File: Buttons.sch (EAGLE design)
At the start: 67 parts, among them J1 AVR_SPI_PROG_3X2TESTPOINTS, T1 SI2301, U1 TCA8418RTWR, U3 ATTINY88-MU

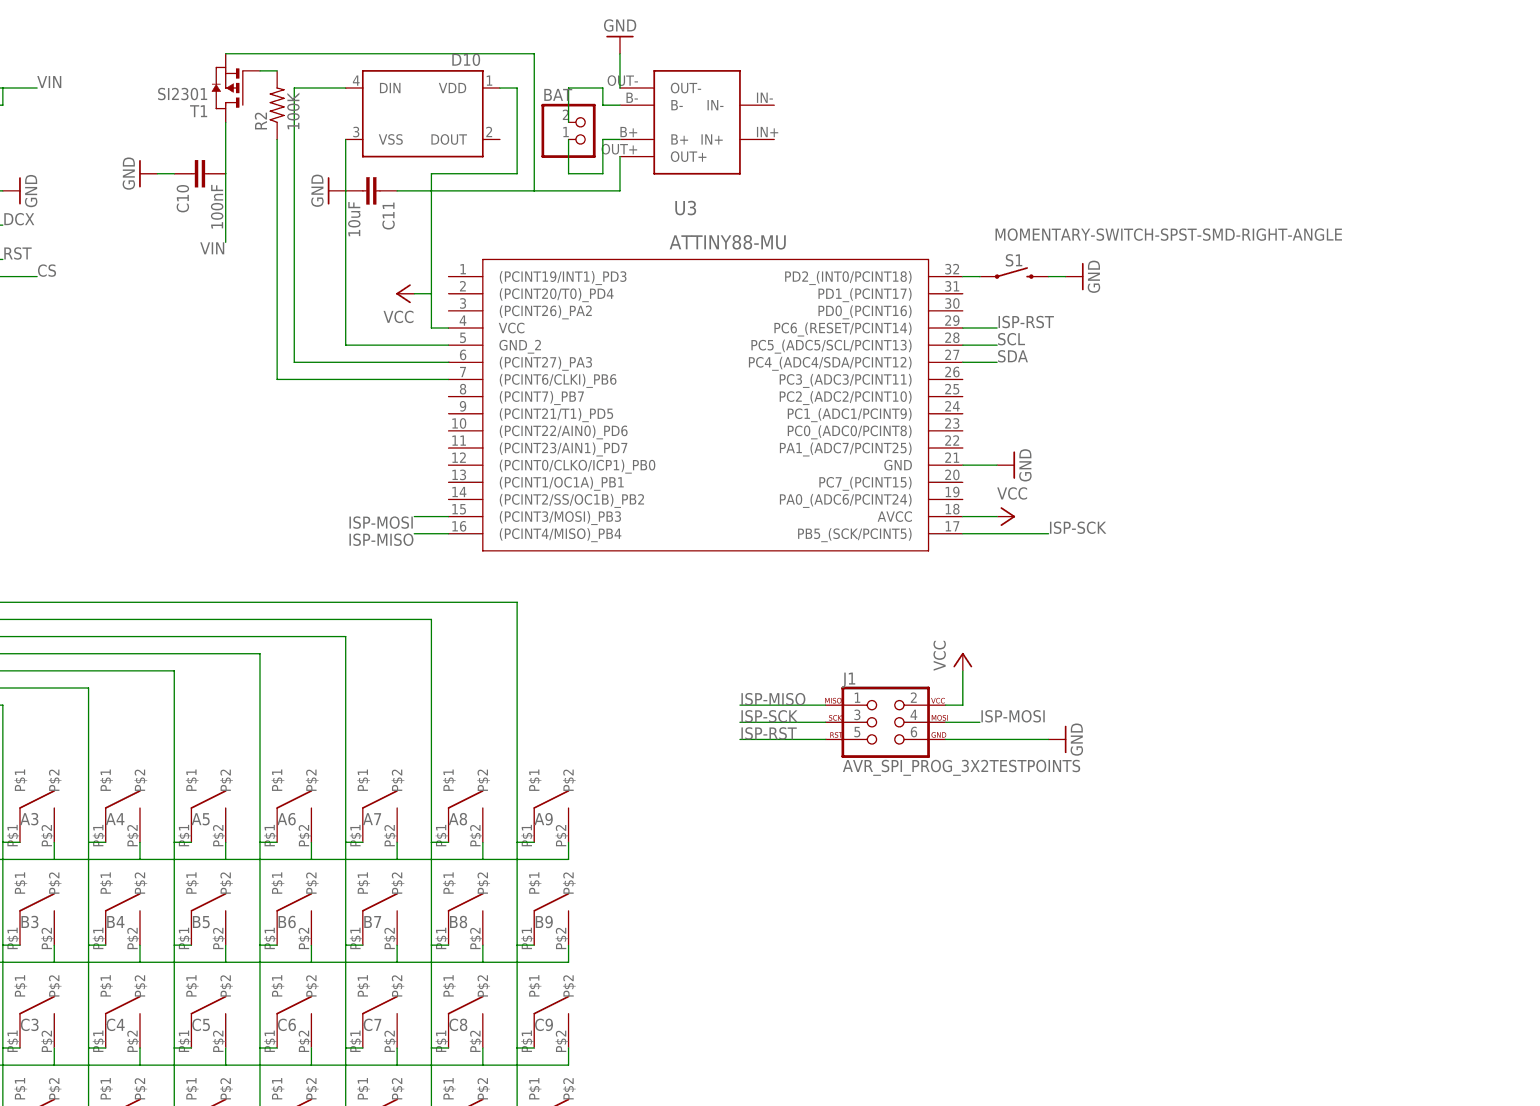
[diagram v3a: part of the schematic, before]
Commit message: changed to atmega328
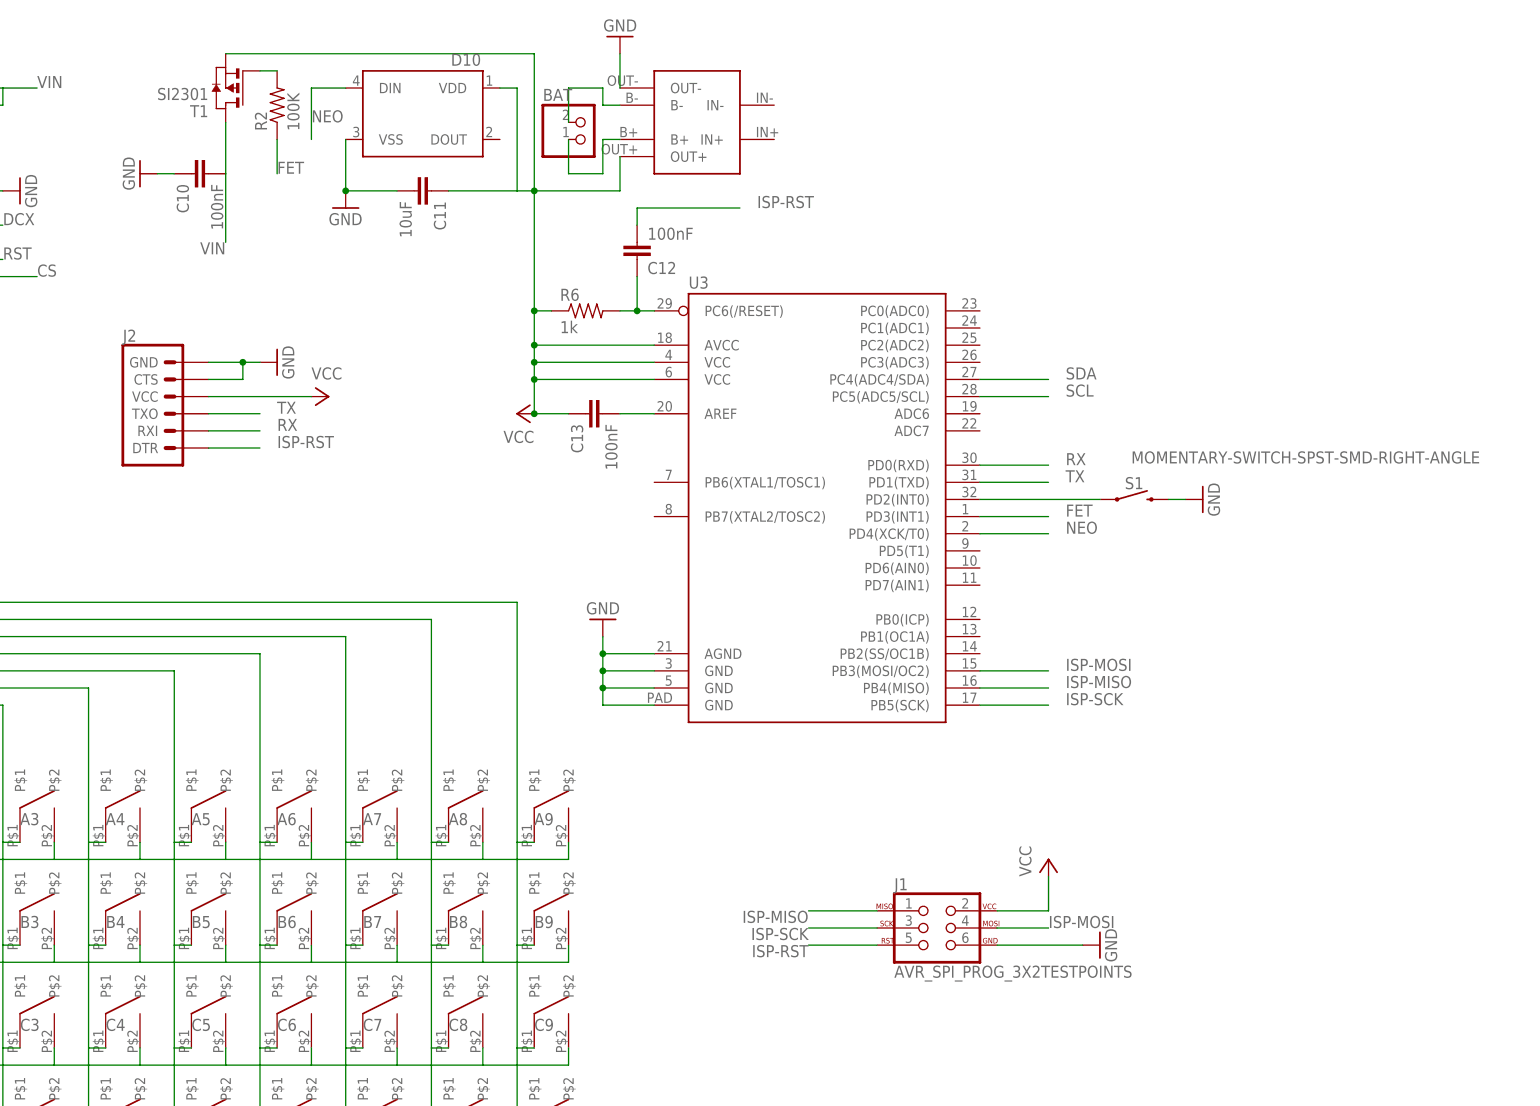
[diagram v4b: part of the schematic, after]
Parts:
- added C12, C13: 100nF, rcl:C-EUC0603K
- added J2: (no value), SparkFun-Connectors:6_PIN_SERIAL_TARGETSILK
- added R6: 1k, SparkFun-Passives:RESISTOR0805-RES
- U3: value ATTINY88-MU -> (none); device attiny88:ATTINY88-MU -> SparkFun-IC-Microcontroller:ATMEGA328P_MLFMLF32
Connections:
- removed net N$19: R2.1, U3.(PCINT6/CLKI)_PB6
- removed net N$2: D10.DIN, U3.(PCINT27)_PA3
- new net FET: R2.1, U3.PD3(INT1)
- new net N$3: C13.2, U3.AREF
- new net N$4: C12.1, R6.2, U3.PC6(/RESET)
- new net NEO: D10.DIN, U3.PD4(XCK/T0)
- new net RX: J2.RXI, U3.PD0(RXD)
- new net TX: J2.TXO, U3.PD1(TXD)
- net GND: now also J2.CTS, J2.GND, U3.AGND, U3.GND@3, U3.GND@5, U3.GND@PAD; no longer U3.GND, U3.GND_2
- net ISP-MISO: now also U3.PB4(MISO); no longer U3.(PCINT4/MISO)_PB4
- net ISP-MOSI: now also U3.PB3(MOSI/OC2); no longer U3.(PCINT3/MOSI)_PB3
- net ISP-RST: now also C12.2, J2.DTR; no longer U3.PC6_(RESET/PCINT14)
- net ISP-SCK: now also U3.PB5(SCK); no longer U3.PB5_(SCK/PCINT5)
- net N$1: now also U3.PD2(INT0); no longer U3.PD2_(INT0/PCINT18)
- net SCL: now also U3.PC5(ADC5/SCL); no longer U3.PC5_(ADC5/SCL/PCINT13)
- net SDA: now also U3.PC4(ADC4/SDA); no longer U3.PC4_(ADC4/SDA/PCINT12)
- net VCC: now also C13.1, J2.VCC, R6.1, U3.VCC@4, U3.VCC@6; no longer U3.VCC
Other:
- moved on the sheet: C11, J1, S1

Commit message: fixed issue with power button footprint
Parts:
- removed S1: MOMENTARY-SWITCH-SPST-SMD-RIGHT-ANGLE, SparkFun-Switches:MOMENTARY-SWITCH-SPST-SMD-RIGHT-ANGLE
- added S2: EVQ-P7L01P, switch-panasonic:EVQ-P7L01P
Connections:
- net GND: now also S2.S1; no longer S1.2
- net N$1: now also S2.P; no longer S1.1
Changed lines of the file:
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@@
 <?xml version="1.0" encoding="utf-8"?>
 <!DOCTYPE eagle SYSTEM "eagle.dtd">
-<eagle version="8.3.2">
+<eagle version="8.5.2">
 <drawing>
 <settings>
@@
 <grid distance="0.1" unitdist="inch" unit="inch" style="lines" multiple="1" display="no" altdistance="0.01" altunitdist="inch" altunit="inch"/>
 <layers>
-<layer number="1" name="Top" color="4" fill="1" visible="no" active="no"/>
-<layer number="16" name="Bottom" color="1" fill="1" visible="no" active="no"/>
-<layer number="17" name="Pads" color="2" fill="1" visible="no" active="no"/>
-<layer number="18" name="Vias" color="2" fill="1" visible="no" active="no"/>
-<layer number="19" name="Unrouted" color="6" fill="1" visible="no" active="no"/>
-<layer number="20" name="Dimension" color="15" fill="1" visible="no" active="no"/>
-<layer number="21" name="tPlace" color="7" fill="1" visible="no" active="no"/>
-<layer number="22" name="bPlace" color="7" fill="1" visible="no" active="no"/>
-<layer number="23" name="tOrigins" color="15" fill="1" visible="no" active="no"/>
-<layer number="24" name="bOrigins" color="15" fill="1" visible="no" active="no"/>
-<layer number="25" name="tNames" color="7" fill="1" visible="no" active="no"/>
-<layer number="26" name="bNames" color="7" fill="1" visible="no" active="no"/>
-<layer number="27" name="tValues" color="7" fill="1" visible="no" active="no"/>
-<layer number="28" name="bValues" color="7" fill="1" visible="no" active="no"/>
+<layer number="1" name="Top" color="4" fill="1" visible="yes" active="no"/>
+<layer number="16" name="Bottom" color="1" fill="1" visible="yes" active="no"/>
+<layer number="17" name="Pads" color="2" fill="1" visible="yes" active="no"/>
+<layer number="18" name="Vias" color="2" fill="1" visible="yes" active="no"/>
+<layer number="19" name="Unrouted" color="6" fill="1" visible="yes" active="no"/>
+<layer number="20" name="Dimension" color="15" fill="1" visible="yes" active="no"/>
+<layer number="21" name="tPlace" color="7" fill="1" visible="yes" active="no"/>
+<layer number="22" name="bPlace" color="7" fill="1" visible="yes" active="no"/>
+<layer number="23" name="tOrigins" color="15" fill="1" visible="yes" active="no"/>
+<layer number="24" name="bOrigins" color="15" fill="1" visible="yes" active="no"/>
+<layer number="25" name="tNames" color="7" fill="1" visible="yes" active="no"/>
+<layer number="26" name="bNames" color="7" fill="1" visible="yes" active="no"/>
+<layer number="27" name="tValues" color="7" fill="1" visible="yes" active="no"/>
+<layer number="28" name="bValues" color="7" fill="1" visible="yes" active="no"/>
 <layer number="29" name="tStop" color="7" fill="3" visible="no" active="no"/>
 <layer number="30" name="bStop" color="7" fill="6" visible="no" active="no"/>
@@
 <layer number="35" name="tGlue" color="7" fill="4" visible="no" active="no"/>
 <layer number="36" name="bGlue" color="7" fill="5" visible="no" active="no"/>
-<layer number="37" name="tTest" color="7" fill="1" visible="no" active="no"/>
-<layer number="38" name="bTest" color="7" fill="1" visible="no" active="no"/>
+<layer number="37" name="tTest" color="7" fill="1" visible="yes" active="no"/>
+<layer number="38" name="bTest" color="7" fill="1" visible="yes" active="no"/>
 <layer number="39" name="tKeepout" color="4" fill="11" visible="no" active="no"/>
 <layer number="40" name="bKeepout" color="1" fill="11" visible="no" active="no"/>
@@
 <layer number="44" name="Drills" color="7" fill="1" visible="no" active="no"/>
 <layer number="45" name="Holes" color="7" fill="1" visible="no" active="no"/>
-<layer number="46" name="Milling" color="3" fill="1" visible="no" active="no"/>
-<layer number="47" name="Measures" color="7" fill="1" visible="no" active="no"/>
-<layer number="48" name="Document" color="7" fill="1" visible="no" active="no"/>
-<layer number="49" name="Reference" color="7" fill="1" visible="no" active="no"/>
-<layer number="50" name="dxf" color="7" fill="1" visible="no" active="no"/>
-<layer number="51" name="tDocu" color="7" fill="1" visible="no" active="no"/>
-<layer number="52" name="bDocu" color="7" fill="1" visible="no" active="no"/>
-<layer number="53" name="tGND_GNDA" color="7" fill="1" visible="no" active="no"/>
-<layer number="54" name="bGND_GNDA" color="7" fill="1" visible="no" active="no"/>
-<layer number="56" name="wert" color="7" fill="1" visible="no" active="no"/>
-<layer number="57" name="tCAD" color="7" fill="1" visible="no" active="no"/>
-<layer number="59" name="tCarbon" color="7" fill="1" visible="no" active="no"/>
-<layer number="60" name="bCarbon" color="7" fill="1" visible="no" active="no"/>
+<layer number="46" name="Milling" color="3" fill="1" visible="yes" active="no"/>
+<layer number="47" name="Measures" color="7" fill="1" visible="yes" active="no"/>
+<layer number="48" name="Document" color="7" fill="1" visible="yes" active="no"/>
+<layer number="49" name="Reference" color="7" fill="1" visible="yes" active="no"/>
+<layer number="50" name="dxf" color="7" fill="1" visible="yes" active="no"/>
+<layer number="51" name="tDocu" color="7" fill="1" visible="yes" active="no"/>
+<layer number="52" name="bDocu" color="7" fill="1" visible="yes" active="no"/>
+<layer number="53" name="tGND_GNDA" color="7" fill="1" visible="yes" active="no"/>
+<layer number="54" name="bGND_GNDA" color="7" fill="1" visible="yes" active="no"/>
+<layer number="56" name="wert" color="7" fill="1" visible="yes" active="no"/>
+<layer number="57" name="tCAD" color="7" fill="1" visible="yes" active="no"/>
+<layer number="59" name="tCarbon" color="7" fill="1" visible="yes" active="no"/>
+<layer number="60" name="bCarbon" color="7" fill="1" visible="yes" active="no"/>
 <layer number="90" name="Modules" color="5" fill="1" visible="yes" active="yes"/>
 <layer number="91" name="Nets" color="2" fill="1" visible="yes" active="yes"/>
@@
 <part name="R5" library="SparkFun-Passives" deviceset="RESISTOR" device="0805-RES" value="1k"/>
 <part name="GND7" library="supply1" deviceset="GND" device=""/>
-<part name="S1" library="SparkFun-Switches" library_urn="urn:adsk.eagle:library:535" deviceset="MOMENTARY-SWITCH-SPST" device="-SMD-RIGHT-ANGLE"/>
 <part name="GND11" library="supply1" deviceset="GND" device=""/>
 <part name="P+3" library="supply1" deviceset="VCC" device=""/>
@@
 <part name="P+2" library="supply1" deviceset="VCC" device=""/>
 <part name="GND13" library="supply1" deviceset="GND" device=""/>
+<part name="S2" library="switch-panasonic" deviceset="EVQ-P7L01P" device=""/>
 </parts>
 <sheets>
@@
 <instance part="E9" gate="G$1" x="144.78" y="17.78"/>
 <instance part="E0" gate="G$1" x="30.48" y="17.78"/>
-<instance part="GND1" gate="1" x="241.3" y="124.46" rot="R90"/>
+<instance part="GND1" gate="1" x="251.46" y="121.92" rot="R90"/>
 <instance part="GND2" gate="1" x="114.3" y="167.64"/>
 <instance part="T1" gate="A" x="96.52" y="185.42" rot="R180"/>
@@
 <instance part="R5" gate="G$1" x="-40.64" y="109.22"/>
 <instance part="GND7" gate="1" x="-2.54" y="175.26" rot="R270"/>
-<instance part="S1" gate="G$1" x="231.14" y="124.46" smashed="yes">
-<attribute name="NAME" x="231.14" y="125.984" size="1.778" layer="95" font="vector" align="bottom-center"/>
-<attribute name="VALUE" x="256.54" y="131.572" size="1.778" layer="96" font="vector" align="top-center"/>
-</instance>
 <instance part="GND11" gate="1" x="152.4" y="106.68" rot="R180"/>
 <instance part="P+3" gate="VCC" x="218.44" y="71.12"/>
@@
 <instance part="P+2" gate="VCC" x="111.76" y="139.7" rot="R270"/>
 <instance part="GND13" gate="1" x="104.14" y="144.78" rot="R90"/>
+<instance part="S2" gate="G$1" x="233.68" y="124.46" rot="R270"/>
 </instances>
 <busses>
@@
 </segment>
 <segment>
-<pinref part="S1" gate="G$1" pin="2"/>
-<pinref part="GND1" gate="1" pin="GND"/>
-<wire x1="236.22" y1="124.46" x2="238.76" y2="124.46" width="0.1524" layer="91"/>
-</segment>
-<segment>
 <pinref part="GND12" gate="1" pin="GND"/>
 <wire x1="210.82" y1="58.42" x2="223.52" y2="58.42" width="0.1524" layer="91"/>
@@
 <wire x1="99.06" y1="142.24" x2="99.06" y2="144.78" width="0.1524" layer="91"/>
 <junction x="99.06" y="144.78"/>
+</segment>
+<segment>
+<pinref part="S2" gate="G$1" pin="S1"/>
+<pinref part="GND1" gate="1" pin="GND"/>
+<wire x1="238.76" y1="121.92" x2="248.92" y2="121.92" width="0.1524" layer="91"/>
 </segment>
 </net>
@@
 </segment>
 </net>
-<net name="N$1" class="0">
-<segment>
-<pinref part="S1" gate="G$1" pin="1"/>
-<wire x1="226.06" y1="124.46" x2="208.28" y2="124.46" width="0.1524" layer="91"/>
-<pinref part="U3" gate="U$1" pin="PD2(INT0)"/>
-</segment>
-</net>
 <net name="FET" class="0">
 <segment>
@@
 </segment>
 </net>
+<net name="N$1" class="0">
+<segment>
+<pinref part="U3" gate="U$1" pin="PD2(INT0)"/>
+<pinref part="S2" gate="G$1" pin="P"/>
+<wire x1="208.28" y1="124.46" x2="228.6" y2="124.46" width="0.1524" layer="91"/>
+</segment>
+</net>
